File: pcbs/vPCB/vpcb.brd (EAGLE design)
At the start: 26.3 x 39.4 mm, 39 parts

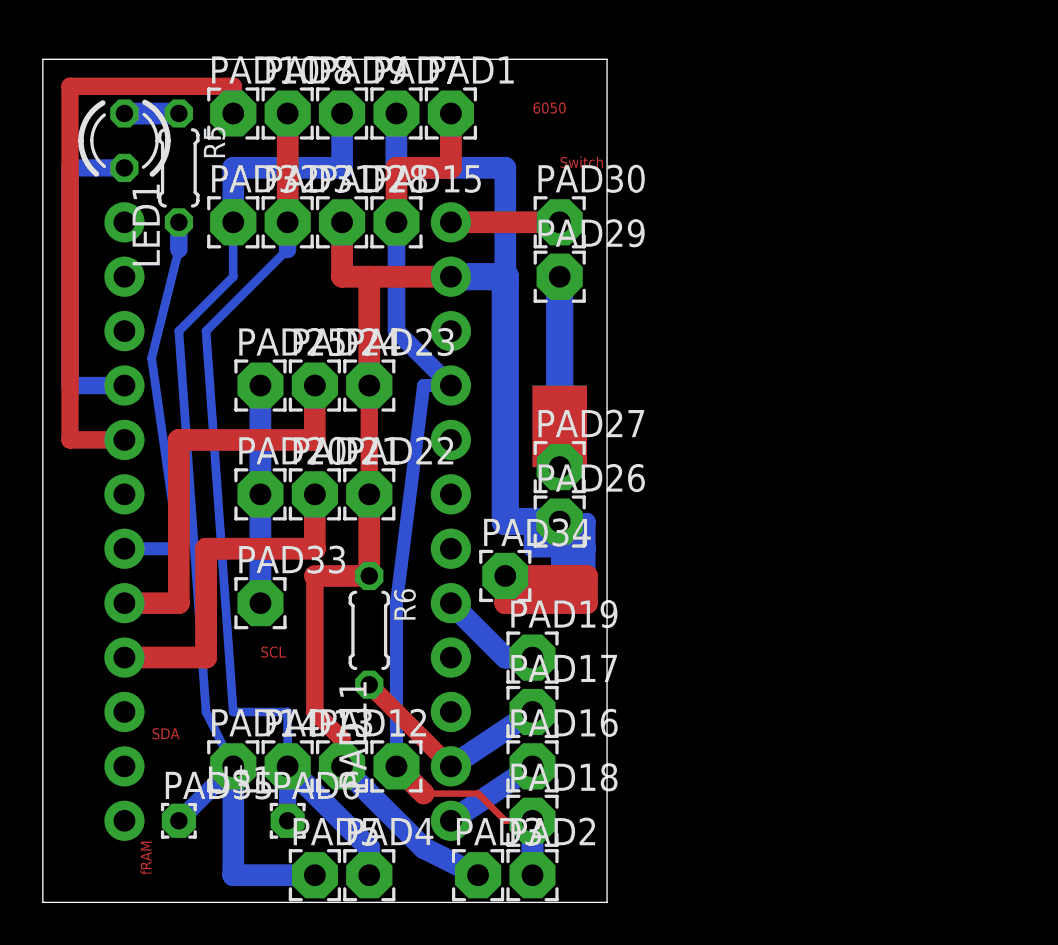
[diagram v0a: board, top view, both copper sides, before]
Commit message: * Making PCM a bit wider to accomodate battery.
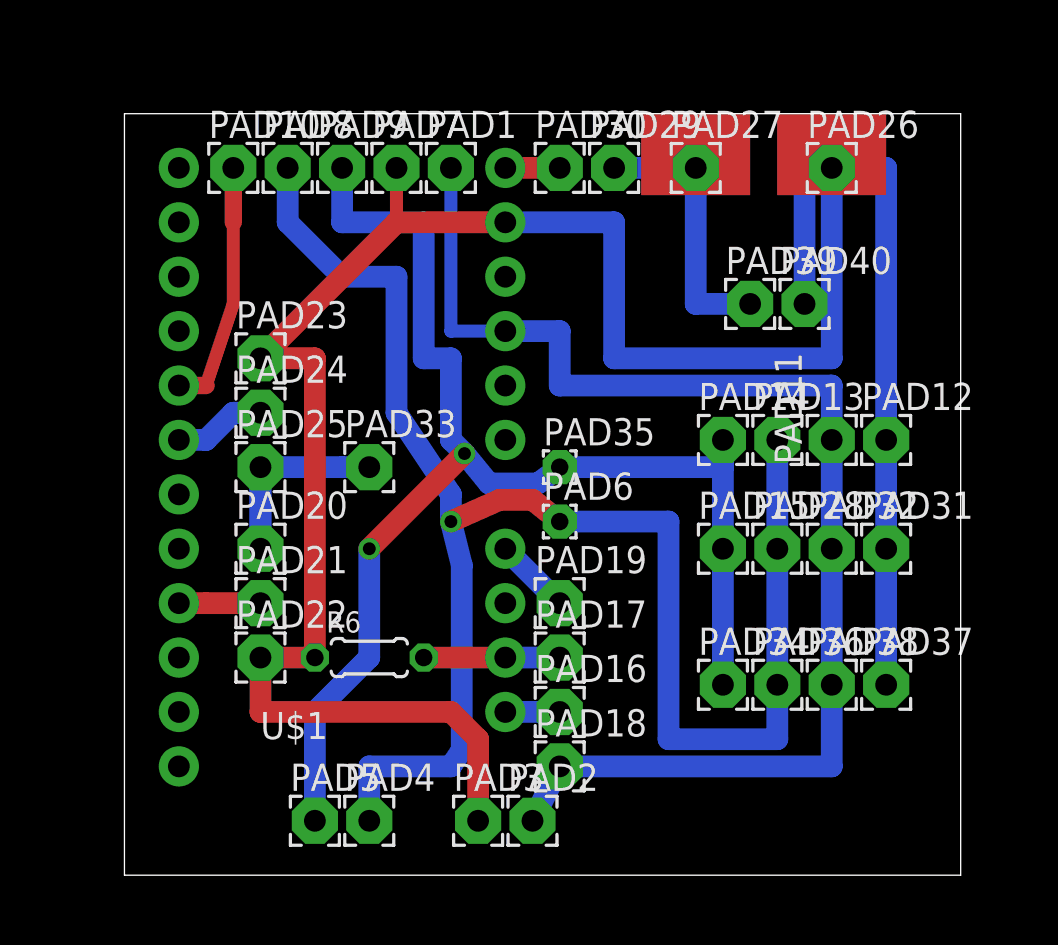
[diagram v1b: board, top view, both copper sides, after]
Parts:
- removed LED1: (no value), led:LED3MM
- removed R5: (no value), resistor:0204/5
- added PAD36, PAD37, PAD38, PAD39, PAD40: (no value), wirepad:2,15/1,0
- U$1: device Joe_SparkFun-Boards:ARDUINO_MINI -> vPCB_Joe_SparkFun-Boards:ARDUINO_MINI
- moved PAD32 31.8 mm to (88.9, 52.1)
- moved PAD31 31.8 mm to (91.4, 52.1)
- moved PAD12 29.6 mm to (91.4, 57.1)
- moved PAD13 27.5 mm to (86.4, 57.1)
- moved PAD14 27.5 mm to (83.8, 57.1)
- moved PAD11 25.4 mm to (88.9, 57.1)
- moved PAD28 25.4 mm to (86.4, 52.1)
- moved PAD35 24.3 mm to (76.2, 55.9)
- moved PAD15 21.6 mm to (83.8, 52.1)
- moved PAD26 20.8 mm to (88.9, 69.8)
- moved PAD6 18.9 mm to (76.2, 53.3)
- moved PAD27 15.3 mm to (82.5, 69.8)
- moved PAD34 11.4 mm to (83.8, 45.7)
- moved PAD22 9.16 mm to (62.2, 47.0)
- moved PAD33 8.13 mm to (67.3, 55.9)
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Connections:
- removed net N$11: U$1.18
- removed net N$13: U$1.15
- removed net N$16: LED1.A, R5.1
- removed net N$18: PAD34.1
- removed net N$23: R5.2, U$1.7
- removed net N$4: PAD16.1, U$1.13
- new net N$20: PAD16.1, U$1.14
- net GND: no longer LED1.K
- net N$1: now also PAD28.1, PAD36.1; no longer PAD31.1
- net N$14: now also U$1.6; no longer U$1.8
- net N$17: now also U$1.15; no longer U$1.14
- net N$19: now also PAD31.1, PAD37.1, PAD40.1; no longer PAD28.1
- net N$2: now also PAD15.1, PAD34.1; no longer PAD32.1
- net N$3: now also PAD32.1, PAD38.1; no longer PAD15.1
- net VCC: now also PAD39.1
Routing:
- net N$1: track 43.8 -> 78.8 mm, vias 0 -> 1
- net N$19: track 84.2 -> 117.5 mm
- net N$23: track 18.0 -> 0.00 mm
- net N$6: track 27.9 -> 11.6 mm
- net N$3: track 45.4 -> 61.3 mm
- net GND: track 15.2 -> 0.00 mm
- net N$2: track 49.4 -> 64.4 mm, vias 0 -> 2
- net N$14: track 19.0 -> 4.34 mm
- net N$15: track 16.5 -> 3.81 mm
- net N$18: track 10.2 -> 0.00 mm
- net N$4: track 4.58 -> 0.00 mm
- net VCC: track 8.89 -> 12.7 mm
- net N$17: track 9.97 -> 6.35 mm
- net N$8: track 10.2 -> 12.7 mm
- net N$20: track 0.00 -> 2.54 mm
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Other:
- board size 26.3 x 39.4 mm -> 39 x 35.5 mm
- board text removed: "6050"
- board text removed: "SCL"
- board text removed: "SDA"
- board text removed: "Switch"
- board text removed: "fRAM"

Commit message: Many refinements to vPCB. - Adding ID, date build - Adding charge point - Adding LED - Adding voltage-test resistors - Fixing battery connector (was around the wrong way) - Adding sufficient space (top/bottom) to slip into 1.5mm trench.
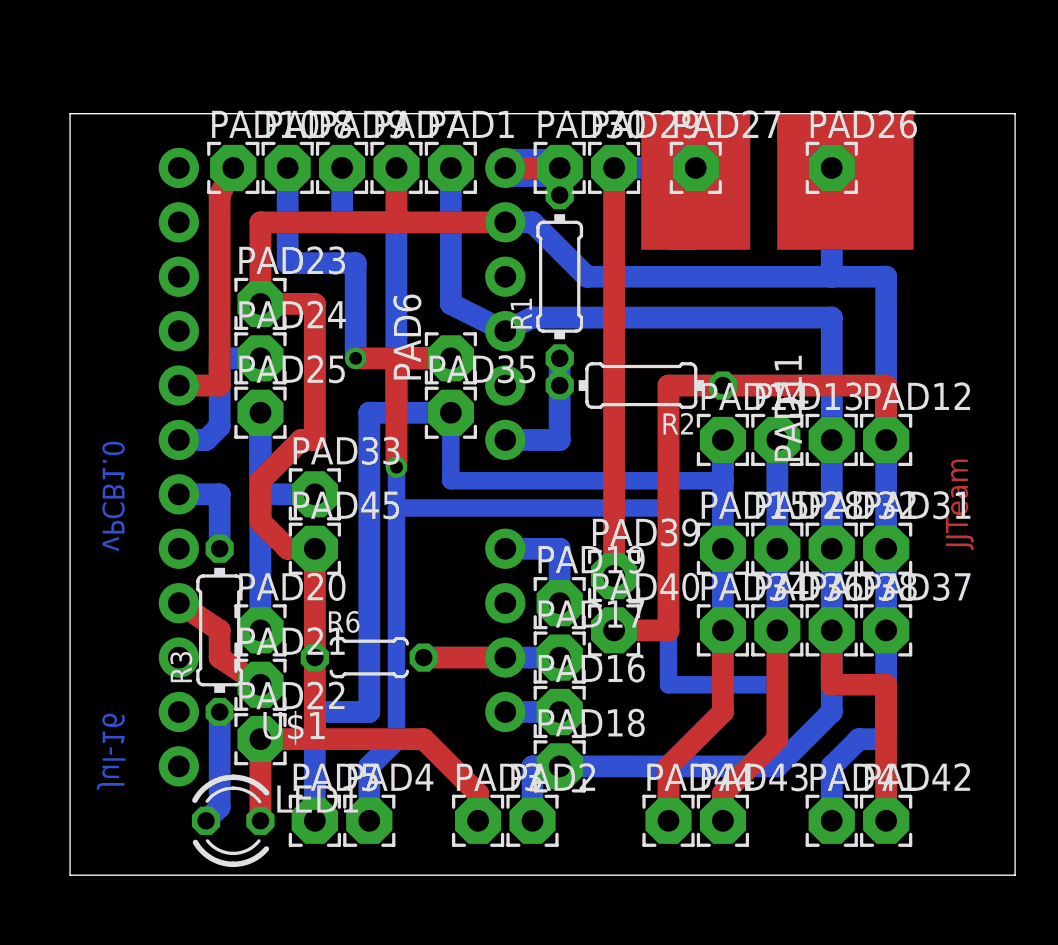
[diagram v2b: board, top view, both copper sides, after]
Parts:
- added LED1: (no value), led:LED3MM
- added PAD41, PAD42, PAD43, PAD44, PAD45: (no value), wirepad:2,15/1,0
- added R1, R2, R3: (no value), resistor:0204/7
- PAD35, PAD6: device wirepad:1,6/0,8 -> wirepad:2,15/1,0
- moved PAD40 17.6 mm to (78.7, 48.3)
- moved PAD39 14.2 mm to (78.7, 50.8)
- moved PAD6 9.16 mm to (71.1, 61.0), turned to 90 degrees
- moved PAD35 5.68 mm to (71.1, 58.4)
- moved PAD20 3.81 mm to (62.2, 48.3)
- moved PAD21 3.81 mm to (62.2, 45.7)
- moved PAD22 3.81 mm to (62.2, 43.2)
- moved PAD33 2.84 mm to (64.8, 54.6)
- moved PAD23 2.54 mm to (62.2, 63.5)
- moved PAD24 2.54 mm to (62.2, 61.0)
- moved PAD25 2.54 mm to (62.2, 58.4)
- moved PAD34 2.54 mm to (83.8, 48.3)
- moved PAD36 2.54 mm to (86.4, 48.3)
- moved PAD37 2.54 mm to (91.4, 48.3)
- moved PAD38 2.54 mm to (88.9, 48.3)
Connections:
- removed net N$19: PAD12.1, PAD22.1, PAD23.1, PAD26.1, PAD3.1, PAD31.1, PAD37.1, PAD40.1, PAD7.1, R6.1, U$1.23
- new net N$11: LED1.A, R3.1
- new net N$13: R3.2, U$1.7
- new net N$16: LED1.K, PAD12.1, PAD22.1, PAD23.1, PAD26.1, PAD3.1, PAD31.1, PAD37.1, PAD40.1, PAD41.1, PAD45.1, PAD7.1, R2.1, R6.1, U$1.23
- net N$1: now also PAD43.1
- net N$10: now also R1.1, R2.2
- net N$2: now also PAD44.1
- net N$3: now also PAD42.1
- net N$5: now also R1.2
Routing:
- net N$16: track 0.00 -> 137.9 mm
- net N$19: track 117.5 -> 0.00 mm
- net N$2: track 64.4 -> 75.3 mm, vias 2 -> 0
- net N$3: track 61.3 -> 72.0 mm
- net VCC: track 12.7 -> 22.9 mm
- net N$1: track 78.8 -> 88.6 mm, vias 1 -> 2
- net N$10: track 0.00 -> 6.35 mm
- net N$11: track 0.00 -> 5.34 mm
- net N$13: track 0.00 -> 4.45 mm
- net N$5: track 2.54 -> 6.35 mm
- net N$8: track 12.7 -> 16.5 mm
- net N$14: track 4.34 -> 7.25 mm
- net N$15: track 3.81 -> 5.85 mm
- net N$12: track 3.59 -> 5.08 mm
- net N$6: track 11.6 -> 12.2 mm
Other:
- board size 39 x 35.5 mm -> 44.1 x 35.5 mm
- board text added: "JJTeam"
- board text added: "Jul-16"
- board text added: "vPCB1.0"

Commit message: * Resolved issue with Air sensor pin arrangement not compatible with vPCB * Resolved issue with Servo +ve and Signal being around the wrong way
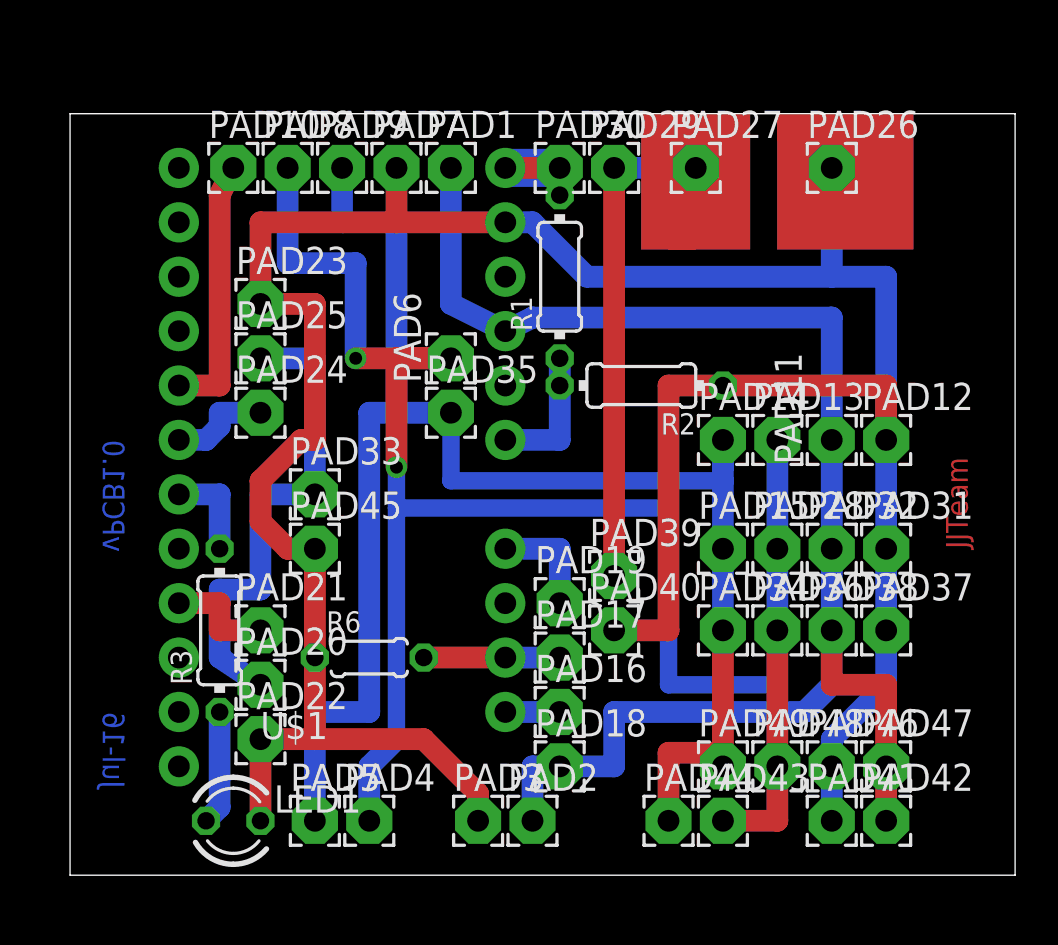
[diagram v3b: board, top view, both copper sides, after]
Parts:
- added PAD46, PAD47, PAD48, PAD49: (no value), wirepad:2,15/1,0
- moved PAD20 2.54 mm to (62.2, 45.7)
- moved PAD21 2.54 mm to (62.2, 48.3)
- moved PAD24 2.54 mm to (62.2, 58.4)
- moved PAD25 2.54 mm to (62.2, 61.0)
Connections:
- net N$1: now also PAD48.1
- net N$16: now also PAD46.1
- net N$2: now also PAD49.1
- net N$3: now also PAD47.1
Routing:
- net N$8: track 16.5 -> 23.2 mm
- net N$14: track 7.25 -> 4.71 mm
- net N$2: track 75.3 -> 77.5 mm
- net N$1: track 88.6 -> 90.1 mm
- net N$15: track 5.85 -> 5.08 mm
- net N$3: track 72.0 -> 72.7 mm
- net N$16: track 137.9 -> 137.2 mm
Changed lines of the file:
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@@
 <layer number="22" name="bPlace" color="7" fill="1" visible="yes" active="yes"/>
 <layer number="23" name="tOrigins" color="15" fill="1" visible="yes" active="yes"/>
-<layer number="24" name="bOrigins" color="15" fill="1" visible="yes" active="yes"/>
+<layer number="24" name="bOrigins" color="15" fill="1" visible="no" active="yes"/>
 <layer number="25" name="tNames" color="7" fill="1" visible="no" active="yes"/>
 <layer number="26" name="bNames" color="7" fill="1" visible="no" active="yes"/>
@@
 <element name="PAD18" library="wirepad" package="2,15/1,0" value="" x="76.2" y="41.91"/>
 <element name="PAD19" library="wirepad" package="2,15/1,0" value="" x="76.2" y="49.53"/>
-<element name="PAD20" library="wirepad" package="2,15/1,0" value="" x="62.23" y="48.26"/>
-<element name="PAD21" library="wirepad" package="2,15/1,0" value="" x="62.23" y="45.72"/>
+<element name="PAD20" library="wirepad" package="2,15/1,0" value="" x="62.23" y="45.72"/>
+<element name="PAD21" library="wirepad" package="2,15/1,0" value="" x="62.23" y="48.26"/>
 <element name="PAD22" library="wirepad" package="2,15/1,0" value="" x="62.23" y="43.18"/>
 <element name="PAD23" library="wirepad" package="2,15/1,0" value="" x="62.23" y="63.5"/>
-<element name="PAD24" library="wirepad" package="2,15/1,0" value="" x="62.23" y="60.96"/>
-<element name="PAD25" library="wirepad" package="2,15/1,0" value="" x="62.23" y="58.42"/>
+<element name="PAD24" library="wirepad" package="2,15/1,0" value="" x="62.23" y="58.42"/>
+<element name="PAD25" library="wirepad" package="2,15/1,0" value="" x="62.23" y="60.96"/>
 <element name="PAD26" library="wirepad" package="2,15/1,0" value="" x="88.9" y="69.85"/>
 <element name="PAD27" library="wirepad" package="2,15/1,0" value="" x="82.55" y="69.85"/>
@@
 <element name="R3" library="resistor" package="0204/7" value="" x="60.325" y="48.26" rot="R90"/>
 <element name="LED1" library="led" package="LED3MM" value="" x="60.96" y="39.37"/>
+<element name="PAD46" library="wirepad" package="2,15/1,0" value="" x="88.9" y="41.91"/>
+<element name="PAD47" library="wirepad" package="2,15/1,0" value="" x="91.44" y="41.91"/>
+<element name="PAD48" library="wirepad" package="2,15/1,0" value="" x="86.36" y="41.91"/>
+<element name="PAD49" library="wirepad" package="2,15/1,0" value="" x="83.82" y="41.91"/>
 </elements>
 <signals>
@@
 <wire x1="74.93" y1="39.37" x2="74.93" y2="41.91" width="1.016" layer="16"/>
 <wire x1="74.93" y1="41.91" x2="76.2" y2="41.91" width="1.016" layer="16"/>
-<wire x1="88.9" y1="57.15" x2="88.9" y2="59.69" width="1.016" layer="16"/>
-<wire x1="88.9" y1="59.69" x2="88.9" y2="62.865" width="1.016" layer="16"/>
+<wire x1="88.9" y1="57.15" x2="88.9" y2="62.865" width="1.016" layer="16"/>
 <wire x1="88.9" y1="62.865" x2="74.93" y2="62.865" width="1.016" layer="16"/>
 <wire x1="74.93" y1="62.865" x2="73.66" y2="62.23" width="1.016" layer="16"/>
@@
 <wire x1="88.9" y1="48.26" x2="88.9" y2="52.07" width="1.016" layer="16"/>
 <contactref element="PAD42" pad="1"/>
-<wire x1="91.44" y1="39.37" x2="91.44" y2="45.72" width="1.016" layer="1"/>
+<wire x1="91.44" y1="41.91" x2="91.44" y2="45.72" width="1.016" layer="1"/>
 <wire x1="91.44" y1="45.72" x2="88.9" y2="45.72" width="1.016" layer="1"/>
 <wire x1="88.9" y1="45.72" x2="88.9" y2="48.26" width="1.016" layer="1"/>
-<wire x1="76.2" y1="41.91" x2="86.36" y2="41.91" width="1.016" layer="16"/>
-<wire x1="86.36" y1="41.91" x2="88.9" y2="44.45" width="1.016" layer="16"/>
-<wire x1="88.9" y1="44.45" x2="88.9" y2="48.26" width="1.016" layer="16"/>
+<wire x1="76.2" y1="41.91" x2="78.74" y2="41.91" width="1.016" layer="16"/>
+<wire x1="78.74" y1="41.91" x2="78.74" y2="44.45" width="1.016" layer="16"/>
+<wire x1="78.74" y1="44.45" x2="87.63" y2="44.45" width="1.016" layer="16"/>
+<wire x1="87.63" y1="44.45" x2="88.9" y2="45.72" width="1.016" layer="16"/>
+<wire x1="88.9" y1="45.72" x2="88.9" y2="48.26" width="1.016" layer="16"/>
+<contactref element="PAD47" pad="1"/>
+<wire x1="91.44" y1="41.91" x2="91.44" y2="39.37" width="1.016" layer="1"/>
 </signal>
 <signal name="N$5">
@@
 <contactref element="PAD8" pad="1"/>
 <contactref element="PAD43" pad="1"/>
-<wire x1="83.82" y1="39.37" x2="83.82" y2="40.64" width="1.016" layer="1"/>
-<wire x1="83.82" y1="40.64" x2="86.36" y2="43.18" width="1.016" layer="1"/>
-<wire x1="86.36" y1="43.18" x2="86.36" y2="48.26" width="1.016" layer="1"/>
+<wire x1="83.82" y1="39.37" x2="86.36" y2="39.37" width="1.016" layer="1"/>
+<wire x1="86.36" y1="41.91" x2="86.36" y2="48.26" width="1.016" layer="1"/>
 <wire x1="67.31" y1="39.37" x2="67.31" y2="41.91" width="1.016" layer="16"/>
 <wire x1="67.31" y1="41.91" x2="68.58" y2="43.18" width="1.016" layer="16"/>
@@
 <via x="68.58" y="55.88" extent="1-16" drill="0.6" shape="square"/>
 <via x="66.675" y="60.96" extent="1-16" drill="0.6" shape="square"/>
+<contactref element="PAD48" pad="1"/>
+<wire x1="86.36" y1="41.91" x2="86.36" y2="39.37" width="1.016" layer="1"/>
 </signal>
 <signal name="N$2">
@@
 <wire x1="68.58" y1="58.42" x2="71.12" y2="58.42" width="1.016" layer="16"/>
 <contactref element="PAD44" pad="1"/>
-<wire x1="81.28" y1="39.37" x2="81.28" y2="41.91" width="1.016" layer="1"/>
-<wire x1="81.28" y1="41.91" x2="83.82" y2="44.45" width="1.016" layer="1"/>
-<wire x1="83.82" y1="44.45" x2="83.82" y2="48.26" width="1.016" layer="1"/>
+<wire x1="81.28" y1="39.37" x2="81.28" y2="42.545" width="1.016" layer="1"/>
+<wire x1="81.28" y1="42.545" x2="83.82" y2="42.545" width="1.016" layer="1"/>
+<wire x1="83.82" y1="42.545" x2="83.82" y2="48.26" width="1.016" layer="1"/>
 <wire x1="71.12" y1="58.42" x2="71.12" y2="55.245" width="0.8128" layer="16"/>
 <wire x1="71.12" y1="55.245" x2="83.82" y2="55.245" width="0.8128" layer="16"/>
@@
 <wire x1="67.31" y1="44.45" x2="67.31" y2="58.42" width="1.016" layer="16"/>
 <wire x1="67.31" y1="58.42" x2="68.58" y2="58.42" width="1.016" layer="16"/>
+<contactref element="PAD49" pad="1"/>
+<wire x1="83.82" y1="41.91" x2="83.82" y2="42.545" width="1.016" layer="1"/>
 </signal>
 <signal name="GND">
@@
 <contactref element="PAD20" pad="1"/>
 <contactref element="PAD33" pad="1"/>
-<wire x1="62.23" y1="48.26" x2="62.23" y2="58.42" width="1.016" layer="16"/>
-<wire x1="62.23" y1="58.42" x2="62.23" y2="54.61" width="1.016" layer="16"/>
+<wire x1="62.23" y1="60.96" x2="64.77" y2="60.96" width="1.016" layer="16"/>
+<wire x1="64.77" y1="60.96" x2="64.77" y2="54.61" width="1.016" layer="16"/>
+<wire x1="62.23" y1="45.72" x2="60.325" y2="46.99" width="1.016" layer="16"/>
+<wire x1="60.325" y1="46.99" x2="60.325" y2="50.165" width="1.016" layer="16"/>
+<wire x1="60.325" y1="50.165" x2="62.23" y2="50.165" width="1.016" layer="16"/>
+<wire x1="62.23" y1="50.165" x2="62.23" y2="54.61" width="1.016" layer="16"/>
 <wire x1="62.23" y1="54.61" x2="64.77" y2="54.61" width="1.016" layer="16"/>
 </signal>
@@
 <contactref element="PAD21" pad="1"/>
 <contactref element="U$1" pad="9"/>
-<wire x1="58.42" y1="49.53" x2="60.325" y2="48.26" width="1.016" layer="1"/>
-<wire x1="60.325" y1="48.26" x2="60.325" y2="46.99" width="1.016" layer="1"/>
-<wire x1="60.325" y1="46.99" x2="62.23" y2="45.72" width="1.016" layer="1"/>
+<wire x1="58.42" y1="49.53" x2="60.325" y2="49.53" width="1.016" layer="1"/>
+<wire x1="60.325" y1="49.53" x2="60.325" y2="48.26" width="1.016" layer="1"/>
+<wire x1="60.325" y1="48.26" x2="62.23" y2="48.26" width="1.016" layer="1"/>
 </signal>
 <signal name="N$14">
@@
 <wire x1="58.42" y1="57.15" x2="59.69" y2="57.15" width="1.016" layer="16"/>
 <wire x1="59.69" y1="57.15" x2="60.325" y2="57.785" width="1.016" layer="16"/>
-<wire x1="60.325" y1="57.785" x2="60.325" y2="60.96" width="1.016" layer="16"/>
-<wire x1="60.325" y1="60.96" x2="62.23" y2="60.96" width="1.016" layer="16"/>
+<wire x1="60.325" y1="57.785" x2="60.325" y2="58.42" width="1.016" layer="16"/>
+<wire x1="60.325" y1="58.42" x2="62.23" y2="58.42" width="1.016" layer="16"/>
 </signal>
 <signal name="N$20">
@@
 <contactref element="PAD40" pad="1"/>
 <contactref element="PAD41" pad="1"/>
-<wire x1="88.9" y1="39.37" x2="88.9" y2="41.91" width="1.016" layer="16"/>
-<wire x1="88.9" y1="41.91" x2="90.17" y2="43.18" width="1.016" layer="16"/>
-<wire x1="90.17" y1="43.18" x2="91.44" y2="43.18" width="1.016" layer="16"/>
-<wire x1="91.44" y1="43.18" x2="91.44" y2="48.26" width="1.016" layer="16"/>
+<wire x1="88.9" y1="41.91" x2="88.9" y2="43.18" width="1.016" layer="16"/>
+<wire x1="88.9" y1="43.18" x2="91.44" y2="45.72" width="1.016" layer="16"/>
+<wire x1="91.44" y1="45.72" x2="91.44" y2="48.26" width="1.016" layer="16"/>
 <wire x1="91.44" y1="48.26" x2="91.44" y2="52.07" width="1.016" layer="16"/>
 <wire x1="91.44" y1="52.07" x2="91.44" y2="57.15" width="1.016" layer="16"/>
@@
 <wire x1="81.28" y1="48.26" x2="81.28" y2="59.69" width="1.016" layer="1"/>
 <wire x1="81.28" y1="59.69" x2="83.82" y2="59.69" width="1.016" layer="1"/>
+<contactref element="PAD46" pad="1"/>
+<wire x1="88.9" y1="41.91" x2="88.9" y2="39.37" width="1.016" layer="16"/>
 </signal>
 </signals>
